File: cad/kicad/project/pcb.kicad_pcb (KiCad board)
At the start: 2 copper layers, 97.2 x 42 mm, 6 parts, among them J1 USB_A, J2 USB_C_Receptacle_USB2.0, U4 PiPico

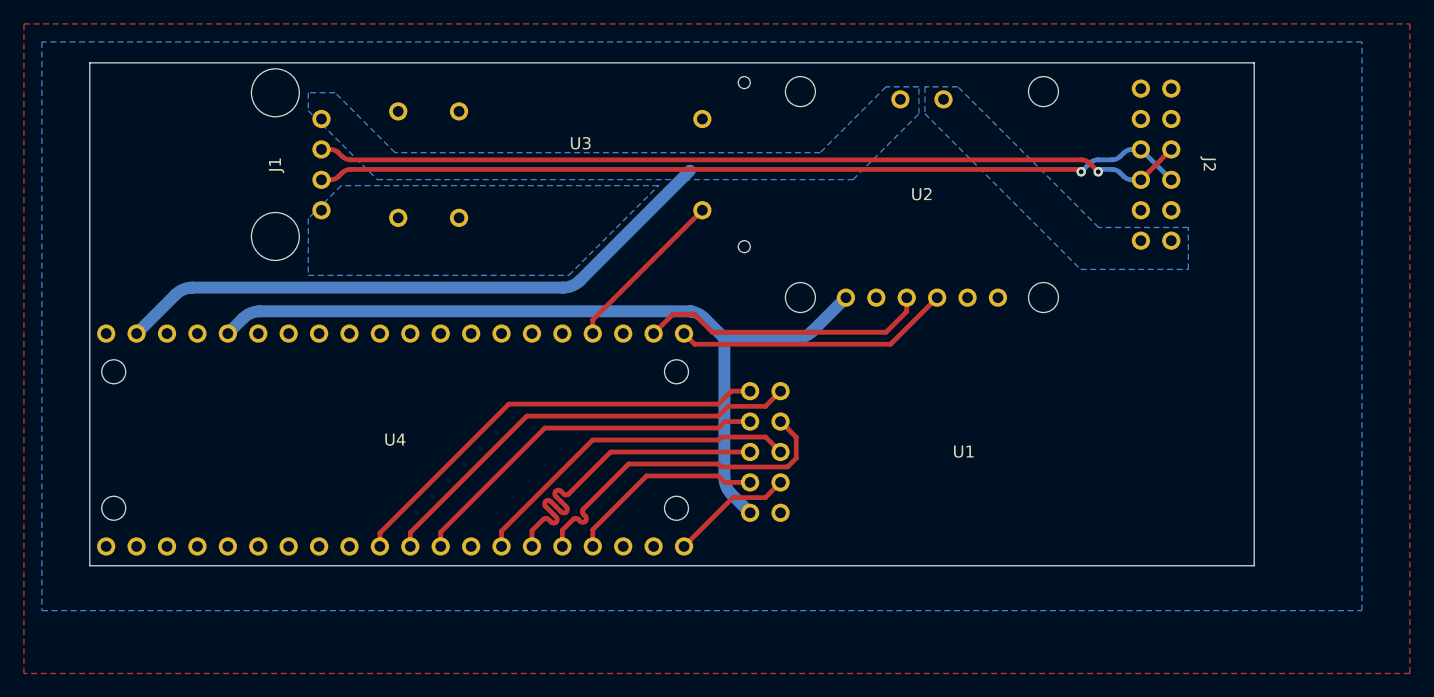
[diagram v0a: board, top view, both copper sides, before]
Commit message: Updated Freecad data
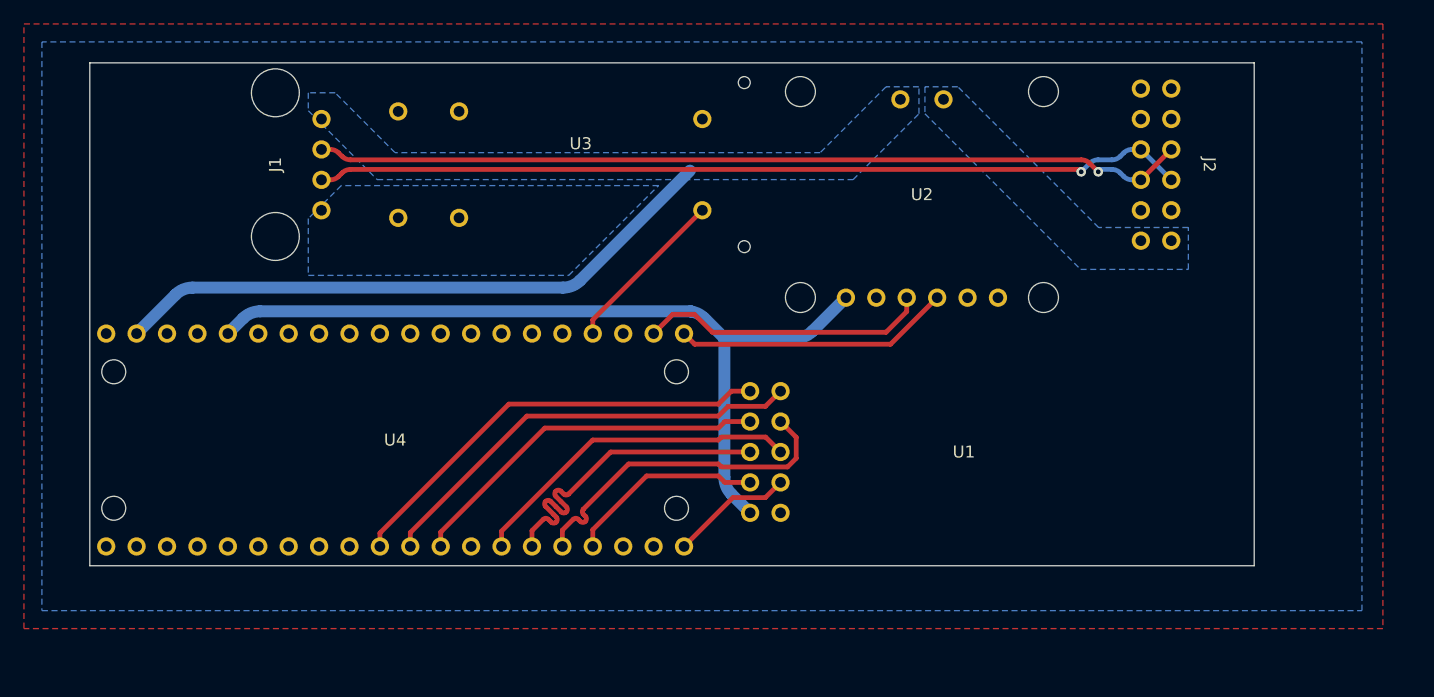
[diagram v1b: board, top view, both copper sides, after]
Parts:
- J1: footprint custom_lib:USB A Port -> somnos_lib:USB A Port
- J2: footprint custom_lib:USB C Port -> somnos_lib:USB C Port
- U1: footprint custom_lib:END28J60 -> somnos_lib:END28J60
- U2: footprint custom_lib:INA219 -> somnos_lib:INA219
- U3: footprint custom_lib:N-MOS_1 -> somnos_lib:N-MOS_1
- U4: footprint custom_lib:PiPico -> somnos_lib:PiPico
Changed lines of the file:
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@@
   (net 42 "/USB_D-")
   (net 43 "/USB_D+")
-  (footprint "custom_lib:N-MOS_1" (layer "F.Cu")
+  (footprint "somnos_lib:N-MOS_1" (layer "F.Cu")
     (at 138.5 80.5 90)
     (property "Sheetfile" "pcb.kicad_sch")
@@
       (net 16 "Net-(U3-TRIG)") (pinfunction "TRIG") (pintype "input"))
   )
-  (footprint "custom_lib:PiPico" (layer "F.Cu")
+  (footprint "somnos_lib:PiPico" (layer "F.Cu")
     (at 123 103.5 90)
     (property "Sheetfile" "pcb.kicad_sch")
@@
       (net 23 "unconnected-(U4-VBUS-Pad40)") (pinfunction "VBUS") (pintype "bidirectional"))
   )
-  (footprint "custom_lib:USB A Port" (layer "F.Cu")
+  (footprint "somnos_lib:USB A Port" (layer "F.Cu")
     (at 110.5 80.5 90)
     (property "Sheetfile" "pcb.kicad_sch")
@@
       (net 2 "Net-(J1-GND)") (pinfunction "GND") (pintype "power_in"))
   )
-  (footprint "custom_lib:END28J60" (layer "F.Cu")
+  (footprint "somnos_lib:END28J60" (layer "F.Cu")
     (at 152.65 104.5 180)
     (property "Sheetfile" "pcb.kicad_sch")
@@
       (net 33 "Net-(U1-CLK)") (pinfunction "CLK") (pintype "bidirectional"))
   )
-  (footprint "custom_lib:INA219" (layer "F.Cu")
+  (footprint "somnos_lib:INA219" (layer "F.Cu")
     (at 167 83)
     (property "Sheetfile" "pcb.kicad_sch")
@@
       (net 7 "Net-(U2-SDA)") (pinfunction "SDA") (pintype "bidirectional"))
   )
-  (footprint "custom_lib:USB C Port" (layer "F.Cu")
+  (footprint "somnos_lib:USB C Port" (layer "F.Cu")
     (at 191 80.5 -90)
     (property "Sheetfile" "pcb.kicad_sch")
@@
       (pts
         (xy 92 68.75)
-        (xy 207.75 68.75)
-        (xy 207.75 123)
-        (xy 92 123)
+        (xy 205.5 68.75)
+        (xy 205.5 119.25)
+        (xy 92 119.25)
       )
     )
